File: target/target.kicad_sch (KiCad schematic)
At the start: 68 parts, among them J1 USB_C_Receptacle_USB2.0, J2 Conn_01x08, J3 Conn_01x03, SW1 SW_Push, SW2 SW_Push, SW3 SW_Push, SW4 SW_Push, SW5 SW_Push, SW6 SW_Push, U1 STM32F103C8Tx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

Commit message: First route
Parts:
- removed J2: Conn_01x08, Connector_PinHeader_2.54mm:PinHeader_1x08_P2.54mm_Vertical, symbol Connector_Generic:Conn_01x08
- removed TP14, TP15, TP16, TP17, TP18, TP19: TP, TestPoint:TestPoint_Bridge_Pitch2.54mm_Drill1.3mm, symbol Connector:TestPoint
- added JP1: SolderJumper_3_Bridged12, Jumper:SolderJumper-3_P1.3mm_Bridged12_RoundedPad1.0x1.5mm, symbol Jumper:SolderJumper_3_Bridged12
- J3: footprint Connector_PinHeader_2.54mm:PinHeader_1x03_P2.54mm_Vertical -> Connector_PinHeader_2.54mm:PinHeader_1x03_P2.54mm_Vertical_SMD_Pin1Left
- TP1, TP10, TP11, TP2, TP3, TP4, TP5, TP6, TP7, TP8, TP9: footprint TestPoint:TestPoint_Bridge_Pitch2.54mm_Drill1.3mm -> TP:TestPoint_CLIP
- TP12, TP13: value TP -> TestPoint; footprint TestPoint:TestPoint_Bridge_Pitch2.54mm_Drill1.3mm -> TP:TestPoint_CLIP
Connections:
- net +3.3V: now also JP1.3 (B)
- net GND: now also TP12.1, TP13.1
- net VMCU: now also JP1.1 (A); no longer U1.9 (VDDA)
- net at R16.2, SW3.2, TP6.1: now also U1.20 (PB2); no longer U1.18 (PB0)
- net at R19.2, SW6.2, TP11.1: now also U1.46 (PB9); no longer U1.39 (PB3)
- net at R10.1, U3.7 (~{WC}): now also U1.16 (PA6); no longer U1.38 (PA15)
- net at R10.2: now also U1.17 (PA7); no longer U1.29 (PA8)
- net at R17.2, SW4.2, TP9.1: now also U1.41 (PB5); no longer U1.19 (PB1)
- net at R18.2, SW5.2, TP10.1: now also U1.45 (PB8); no longer U1.20 (PB2)
- net at U1.14 (PA4): now also R11.1, U4.7 (~{WC}); no longer TP12.1
- net at U1.15 (PA5): now also R11.2; no longer TP13.1
- net at U1.33 (PA12): no longer R11.2
- new net: JP1.2 (C), U1.9 (VDDA)
- now unconnected: U1.32 (PA11)
- no-connect marks 8 -> 23
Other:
- moved on the sheet: C8, R10, R11

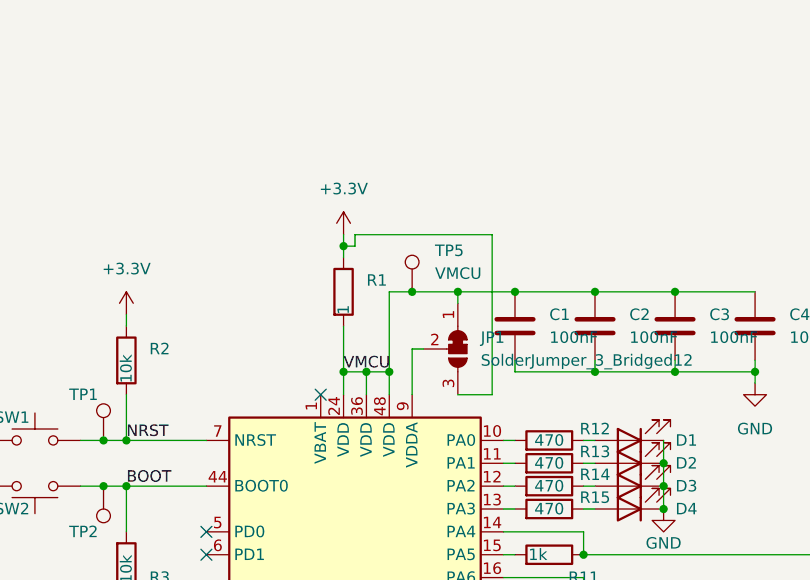
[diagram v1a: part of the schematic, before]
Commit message: Rerouted and less violations
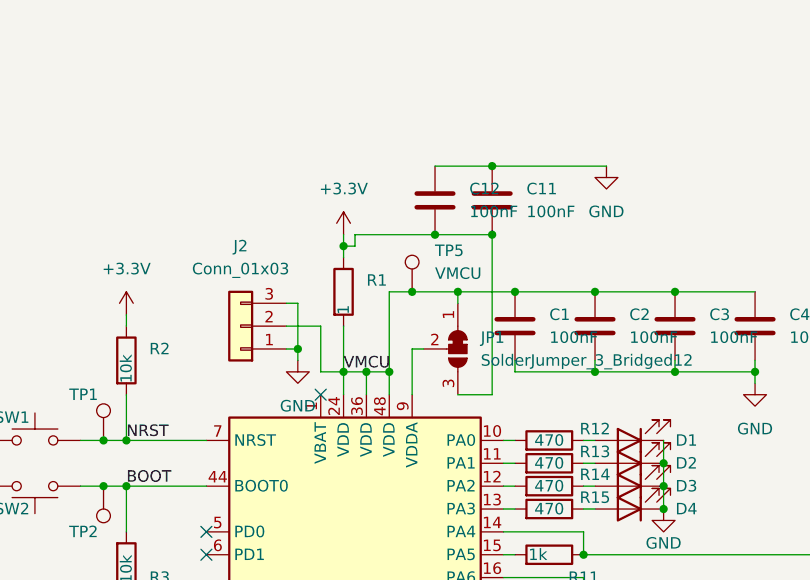
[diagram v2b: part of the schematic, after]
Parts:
- added C11, C12: 100nF, Capacitor_SMD:C_0603_1608Metric, symbol Device:C
- added J2: Conn_01x03, Connector_PinHeader_2.54mm:PinHeader_1x03_P2.54mm_Vertical_SMD_Pin1Left, symbol Connector_Generic:Conn_01x03
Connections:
- net +3.3V: now also C11.2, C12.2
- net GND: now also C11.1, C12.1, J2.1 (Pin_1), J2.3 (Pin_3)
- net VMCU: now also J2.2 (Pin_2)
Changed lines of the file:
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@@
   (junction (at 147.32 46.99) (diameter 0) (color 0 0 0 0)
   )
+  (junction (at 163.83 38.1) (diameter 0) (color 0 0 0 0)
+  )
   (junction (at 181.61 102.87) (diameter 0) (color 0 0 0 0)
   )
@@
   (junction (at 107.95 101.6) (diameter 0) (color 0 0 0 0)
   )
+  (junction (at 157.48 45.72) (diameter 0) (color 0 0 0 0)
+  )
   (junction (at 120.65 73.66) (diameter 0) (color 0 0 0 0)
   )
@@
   (junction (at 123.19 73.66) (diameter 0) (color 0 0 0 0)
   )
+  (junction (at 163.83 45.72) (diameter 0) (color 0 0 0 0)
+  )
   (junction (at 182.88 73.66) (diameter 0) (color 0 0 0 0)
   )
@@
   )
   (junction (at 53.34 63.5) (diameter 0) (color 0 0 0 0)
+  )
+  (junction (at 142.24 58.42) (diameter 0) (color 0 0 0 0)
   )
   (junction (at 46.99 63.5) (diameter 0) (color 0 0 0 0)
@@
     (stroke (width 0) (type default))
   )
+  (wire (pts (xy 157.48 38.1) (xy 163.83 38.1))
+    (stroke (width 0) (type default))
+  )
   (wire (pts (xy 210.82 121.92) (xy 207.01 121.92))
     (stroke (width 0) (type default))
@@
     (stroke (width 0) (type default))
   )
+  (wire (pts (xy 142.24 59.69) (xy 142.24 58.42))
+    (stroke (width 0) (type default))
+  )
   (wire (pts (xy 120.65 68.58) (xy 123.19 68.58))
     (stroke (width 0) (type default))
@@
     (stroke (width 0) (type default))
   )
+  (wire (pts (xy 140.97 53.34) (xy 142.24 53.34))
+    (stroke (width 0) (type default))
+  )
   (wire (pts (xy 181.61 93.98) (xy 181.61 95.25))
     (stroke (width 0) (type default))
@@
     (stroke (width 0) (type default))
   )
+  (wire (pts (xy 163.83 38.1) (xy 176.53 38.1))
+    (stroke (width 0) (type default))
+  )
   (wire (pts (xy 123.19 86.36) (xy 123.19 87.63))
     (stroke (width 0) (type default))
@@
     (stroke (width 0) (type default))
   )
+  (wire (pts (xy 140.97 55.88) (xy 144.78 55.88))
+    (stroke (width 0) (type default))
+  )
   (wire (pts (xy 186.69 148.59) (xy 196.85 148.59))
     (stroke (width 0) (type default))
@@
     (stroke (width 0) (type default))
   )
+  (wire (pts (xy 144.78 60.96) (xy 147.32 60.96))
+    (stroke (width 0) (type default))
+  )
   (wire (pts (xy 181.61 102.87) (xy 181.61 104.14))
     (stroke (width 0) (type default))
@@
     (stroke (width 0) (type default))
   )
+  (wire (pts (xy 157.48 45.72) (xy 148.59 45.72))
+    (stroke (width 0) (type default))
+  )
   (wire (pts (xy 182.88 71.12) (xy 182.88 73.66))
     (stroke (width 0) (type default))
@@
     (stroke (width 0) (type default))
   )
+  (wire (pts (xy 142.24 53.34) (xy 142.24 58.42))
+    (stroke (width 0) (type default))
+  )
   (wire (pts (xy 208.28 102.87) (xy 208.28 104.14))
     (stroke (width 0) (type default))
@@
     (stroke (width 0) (type default))
   )
-  (wire (pts (xy 163.83 45.72) (xy 148.59 45.72))
+  (wire (pts (xy 163.83 45.72) (xy 157.48 45.72))
     (stroke (width 0) (type default))
   )
@@
     (stroke (width 0) (type default))
   )
+  (wire (pts (xy 142.24 58.42) (xy 140.97 58.42))
+    (stroke (width 0) (type default))
+  )
   (wire (pts (xy 186.69 119.38) (xy 186.69 114.3))
     (stroke (width 0) (type default))
@@
   )
   (wire (pts (xy 110.49 104.14) (xy 127 104.14))
+    (stroke (width 0) (type default))
+  )
+  (wire (pts (xy 144.78 55.88) (xy 144.78 60.96))
     (stroke (width 0) (type default))
   )
@@
         (path "/511886a0-9235-416a-a52c-0f086aa6e059"
           (reference "JP1") (unit 1)
+        )
+      )
+    )
+  )
+  (symbol (lib_id "Device:C") (at 163.83 41.91 0) (unit 1)
+    (in_bom yes) (on_board yes) (dnp no) (fields_autoplaced)
+    (property "Reference" "C11" (at 167.64 40.64 0)
+      (effects (font (size 1.27 1.27)) (justify left))
+    )
+    (property "Value" "100nF" (at 167.64 43.18 0)
+      (effects (font (size 1.27 1.27)) (justify left))
+    )
+    (property "Footprint" "Capacitor_SMD:C_0603_1608Metric" (at 164.7952 45.72 0)
+      (effects (font (size 1.27 1.27)) hide)
+    )
+    (property "Datasheet" "~" (at 163.83 41.91 0)
+      (effects (font (size 1.27 1.27)) hide)
+    )
+    (property "LCSC" "C14663" (at 163.83 41.91 0)
+      (effects (font (size 1.27 1.27)) hide)
+    )
+    (pin "1")
+    (pin "2")
+    (instances
+      (project "target"
+        (path "/511886a0-9235-416a-a52c-0f086aa6e059"
+          (reference "C11") (unit 1)
         )
       )
@@
     )
   )
+  (symbol (lib_id "Device:C") (at 157.48 41.91 0) (unit 1)
+    (in_bom yes) (on_board yes) (dnp no) (fields_autoplaced)
+    (property "Reference" "C12" (at 161.29 40.64 0)
+      (effects (font (size 1.27 1.27)) (justify left))
+    )
+    (property "Value" "100nF" (at 161.29 43.18 0)
+      (effects (font (size 1.27 1.27)) (justify left))
+    )
+    (property "Footprint" "Capacitor_SMD:C_0603_1608Metric" (at 158.4452 45.72 0)
+      (effects (font (size 1.27 1.27)) hide)
+    )
+    (property "Datasheet" "~" (at 157.48 41.91 0)
+      (effects (font (size 1.27 1.27)) hide)
+    )
+    (property "LCSC" "C14663" (at 157.48 41.91 0)
+      (effects (font (size 1.27 1.27)) hide)
+    )
+    (pin "1")
+    (pin "2")
+    (instances
+      (project "target"
+        (path "/511886a0-9235-416a-a52c-0f086aa6e059"
+          (reference "C12") (unit 1)
+        )
+      )
+    )
+  )
   (symbol (lib_id "Connector:TestPoint") (at 93.98 101.6 90) (mirror x) (unit 1)
     (in_bom yes) (on_board yes) (dnp no)
@@
     )
   )
+  (symbol (lib_id "power:GND") (at 176.53 38.1 0) (unit 1)
+    (in_bom yes) (on_board yes) (dnp no) (fields_autoplaced)
+    (property "Reference" "#PWR015" (at 176.53 44.45 0)
+      (effects (font (size 1.27 1.27)) hide)
+    )
+    (property "Value" "GND" (at 176.53 43.18 0)
+      (effects (font (size 1.27 1.27)))
+    )
+    (property "Footprint" "" (at 176.53 38.1 0)
+      (effects (font (size 1.27 1.27)) hide)
+    )
+    (property "Datasheet" "" (at 176.53 38.1 0)
+      (effects (font (size 1.27 1.27)) hide)
+    )
+    (pin "1")
+    (instances
+      (project "target"
+        (path "/511886a0-9235-416a-a52c-0f086aa6e059"
+          (reference "#PWR015") (unit 1)
+        )
+      )
+    )
+  )
   (symbol (lib_id "power:GND") (at 181.61 113.03 0) (unit 1)
     (in_bom yes) (on_board yes) (dnp no) (fields_autoplaced)
@@
         (path "/511886a0-9235-416a-a52c-0f086aa6e059"
           (reference "#PWR018") (unit 1)
+        )
+      )
+    )
+  )
+  (symbol (lib_id "Connector_Generic:Conn_01x03") (at 135.89 55.88 180) (unit 1)
+    (in_bom yes) (on_board yes) (dnp no) (fields_autoplaced)
+    (property "Reference" "J2" (at 135.89 46.99 0)
+      (effects (font (size 1.27 1.27)))
+    )
+    (property "Value" "Conn_01x03" (at 135.89 49.53 0)
+      (effects (font (size 1.27 1.27)))
+    )
+    (property "Footprint" "Connector_PinHeader_2.54mm:PinHeader_1x03_P2.54mm_Vertical_SMD_Pin1Left" (at 135.89 55.88 0)
+      (effects (font (size 1.27 1.27)) hide)
+    )
+    (property "Datasheet" "~" (at 135.89 55.88 0)
+      (effects (font (size 1.27 1.27)) hide)
+    )
+    (pin "1")
+    (pin "2")
+    (pin "3")
+    (instances
+      (project "target"
+        (path "/511886a0-9235-416a-a52c-0f086aa6e059"
+          (reference "J2") (unit 1)
         )
       )
@@
         )
       )
+    )
+  )
+  (symbol (lib_id "power:GND") (at 142.24 59.69 0) (unit 1)
+    (in_bom yes) (on_board yes) (dnp no) (fields_autoplaced)
+    (property "Reference" "#PWR016" (at 142.24 66.04 0)
+      (effects (font (size 1.27 1.27)) hide)
+    )
+    (property "Value" "GND" (at 142.24 64.77 0)
+      (effects (font (size 1.27 1.27)))
+    )
+    (property "Footprint" "" (at 142.24 59.69 0)
+      (effects (font (size 1.27 1.27)) hide)
+    )
+    (property "Datasheet" "" (at 142.24 59.69 0)
+      (effects (font (size 1.27 1.27)) hide)
+    )
+    (pin "1")
+    (instances
+      (project "target"
+        (path "/511886a0-9235-416a-a52c-0f086aa6e059"
+          (reference "#PWR016") (unit 1)
+        )
+      )

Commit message: Updated text
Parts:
- J2, J3: LCSC (none) -> C780061
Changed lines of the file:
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@@
+      (effects (font (size 1.27 1.27)) hide)
+    )
+    (property "LCSC" "C780061" (at 135.89 55.88 0)
       (effects (font (size 1.27 1.27)) hide)
     )
@@
       (effects (font (size 1.27 1.27)) hide)
     )
+    (property "LCSC" "C780061" (at 170.18 129.54 0)
+      (effects (font (size 1.27 1.27)) hide)
+    )

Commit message: Prod hw
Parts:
- J2, J3: LCSC C780061 -> C5160786
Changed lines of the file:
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@@
       (effects (font (size 1.27 1.27)) hide)
     )
-    (property "LCSC" "C780061" (at 135.89 55.88 0)
+    (property "LCSC" "C5160786" (at 135.89 55.88 0)
       (effects (font (size 1.27 1.27)) hide)
     )
@@
       (effects (font (size 1.27 1.27)) hide)
     )
-    (property "LCSC" "C780061" (at 170.18 129.54 0)
-      (effects (font (size 1.27 1.27)) hide)
-    )
+    (property "LCSC" "C5160786" (at 170.18 129.54 0)
+      (effects (font (size 1.27 1.27)) hide)
+    )
